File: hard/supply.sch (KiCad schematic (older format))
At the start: 13 parts, among them J2 MicroXNJ

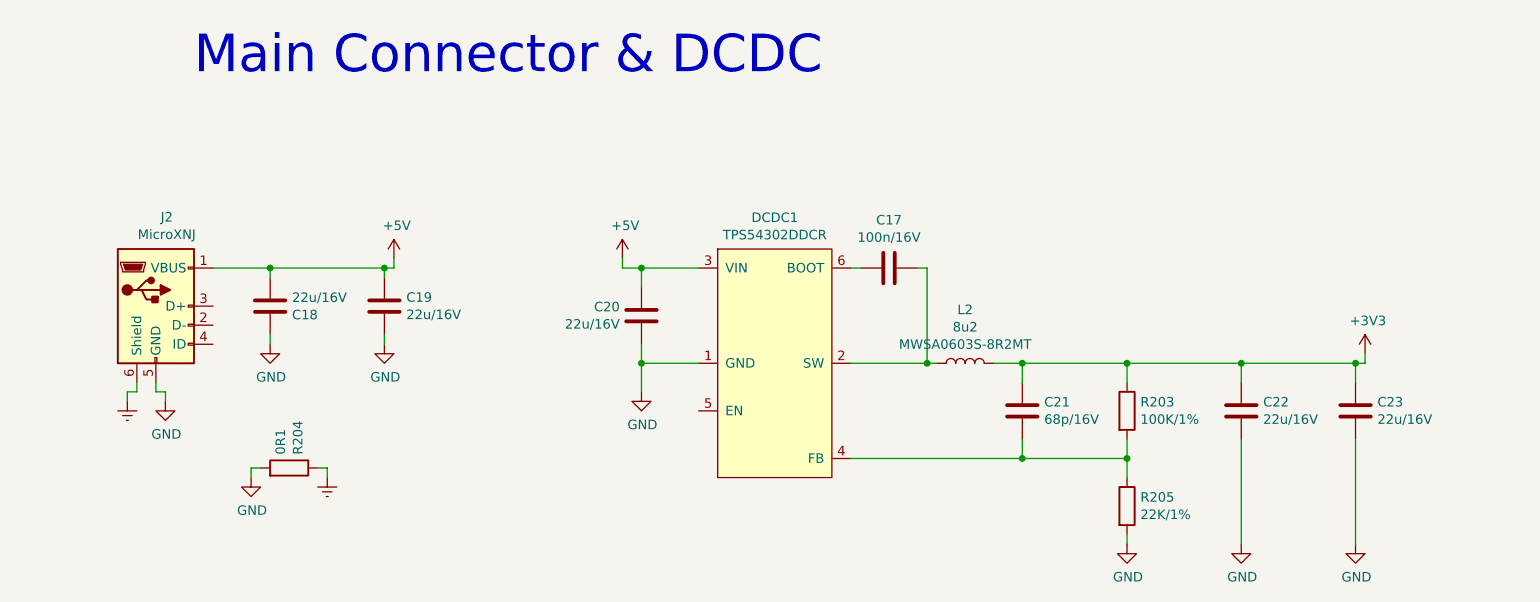
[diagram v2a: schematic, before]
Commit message: general layout update
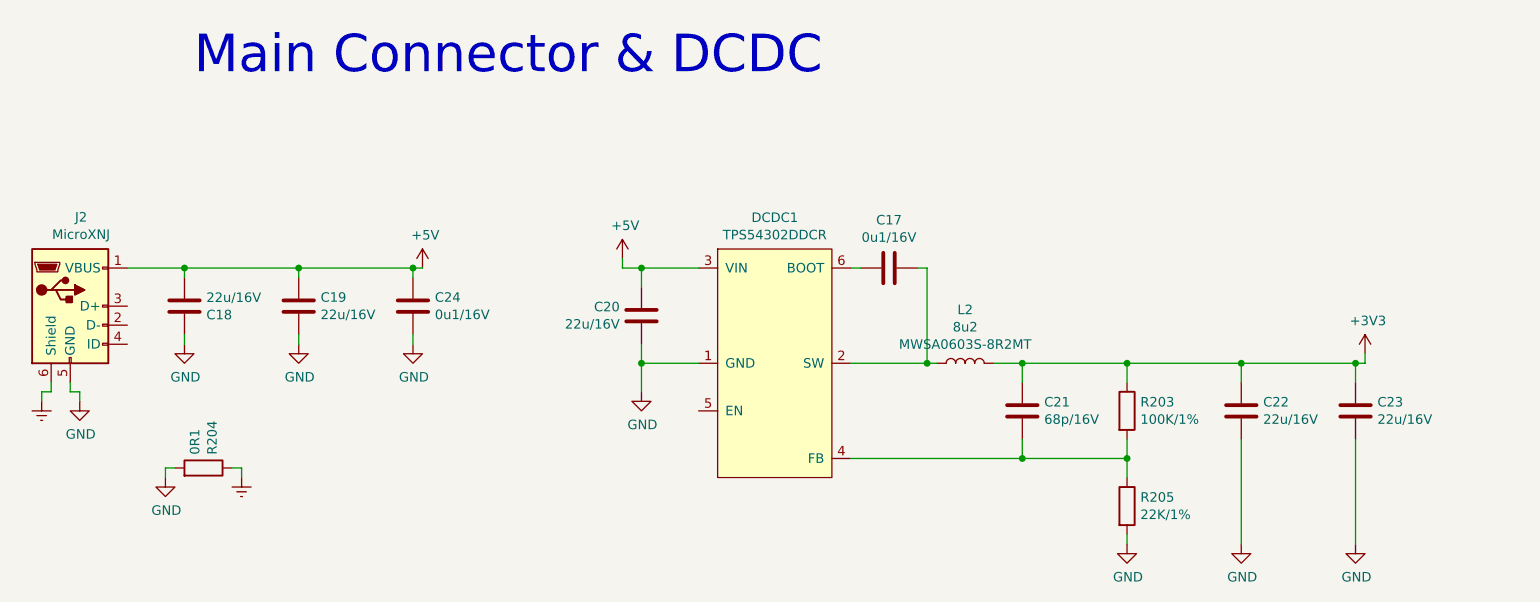
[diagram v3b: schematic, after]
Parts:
- added C24: 0u1/16V, Capacitor_SMD:C_0402_1005Metric, symbol Device:C
- C17: value 100n/16V -> 0u1/16V
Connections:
- net +5V: now also C24.2
- net GND: now also C24.1
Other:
- moved on the sheet: C18, C19, J2, R204
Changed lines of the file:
@@
 P 6750 3400
 F 0 "C17" V 6498 3400 50  0000 C CNN
-F 1 "100n/16V" V 6589 3400 50  0000 C CNN
+F 1 "0u1/16V" V 6589 3400 50  0000 C CNN
 F 2 "Capacitor_SMD:C_0402_1005Metric" H 6788 3250 50  0001 C CNN
 F 3 "~" H 6750 3400 50  0001 C CNN
@@
 L Connector:USB_B_Micro J2
 U 1 1 60567F22
-P 2900 3600
-F 0 "J2" H 2957 4067 50  0000 C CNN
-F 1 "MicroXNJ" H 2957 3976 50  0000 C CNN
-F 2 "led_matrix:Connectors_SHOU HAN_MICRO 4P DIP" H 3050 3550 50  0001 C CNN
-F 3 "1912111437_SHOU-HAN-MICRO-4P-DIP_C456008.pdf" H 3050 3550 50  0001 C CNN
-F 4 "" H 2900 3600 50  0001 C CNN "DigiKey_Part_Number"
-F 5 "" H 2900 3600 50  0001 C CNN "Mouser_Part_Number"
-F 6 "C456008" H 2900 3600 50  0001 C CNN "JLCPCB_Part_Number"
-F 7 "SHOU HAN" H 2900 3600 50  0001 C CNN "MF"
-F 8 "MICRO 4P DIP" H 2900 3600 50  0001 C CNN "MPN"
-F 9 "USB CONNECTORS ROHS" H 2900 3600 50  0001 C CNN "Description"
-	1    2900 3600
+P 2450 3600
+F 0 "J2" H 2507 4067 50  0000 C CNN
+F 1 "MicroXNJ" H 2507 3976 50  0000 C CNN
+F 2 "led_matrix:Connectors_SHOU HAN_MICRO 4P DIP" H 2600 3550 50  0001 C CNN
+F 3 "1912111437_SHOU-HAN-MICRO-4P-DIP_C456008.pdf" H 2600 3550 50  0001 C CNN
+F 4 "" H 2450 3600 50  0001 C CNN "DigiKey_Part_Number"
+F 5 "" H 2450 3600 50  0001 C CNN "Mouser_Part_Number"
+F 6 "C456008" H 2450 3600 50  0001 C CNN "JLCPCB_Part_Number"
+F 7 "SHOU HAN" H 2450 3600 50  0001 C CNN "MF"
+F 8 "MICRO 4P DIP" H 2450 3600 50  0001 C CNN "MPN"
+F 9 "USB CONNECTORS ROHS" H 2450 3600 50  0001 C CNN "Description"
+	1    2450 3600
 	1    0    0    -1
 $EndComp
@@
 L power:+5V #PWR0187
 U 1 1 6056C9AF
-P 4150 3350
-F 0 "#PWR0187" H 4150 3200 50  0001 C CNN
-F 1 "+5V" H 4165 3523 50  0000 C CNN
-F 2 "" H 4150 3350 50  0001 C CNN
-F 3 "" H 4150 3350 50  0001 C CNN
-	1    4150 3350
+P 4300 3400
+F 0 "#PWR0187" H 4300 3250 50  0001 C CNN
+F 1 "+5V" H 4315 3573 50  0000 C CNN
+F 2 "" H 4300 3400 50  0001 C CNN
+F 3 "" H 4300 3400 50  0001 C CNN
+	1    4300 3400
 	1    0    0    -1
 $EndComp
@@
 L power:GND #PWR0194
 U 1 1 6056D447
-P 2950 4100
-F 0 "#PWR0194" H 2950 3850 50  0001 C CNN
-F 1 "GND" H 2955 3927 50  0000 C CNN
-F 2 "" H 2950 4100 50  0001 C CNN
-F 3 "" H 2950 4100 50  0001 C CNN
-	1    2950 4100
+P 2500 4100
+F 0 "#PWR0194" H 2500 3850 50  0001 C CNN
+F 1 "GND" H 2505 3927 50  0000 C CNN
+F 2 "" H 2500 4100 50  0001 C CNN
+F 3 "" H 2500 4100 50  0001 C CNN
+	1    2500 4100
 	1    0    0    -1
 $EndComp
@@
 L Device:R R204
 U 1 1 6056E34B
-P 3600 4450
-F 0 "R204" H 3670 4496 50  0000 L CNN
-F 1 "0R1" H 3670 4405 50  0000 L CNN
-F 2 "Resistor_SMD:R_0805_2012Metric" V 3530 4450 50  0001 C CNN
-F 3 "~" H 3600 4450 50  0001 C CNN
-	1    3600 4450
+P 3150 4450
+F 0 "R204" H 3220 4496 50  0000 L CNN
+F 1 "0R1" H 3220 4405 50  0000 L CNN
+F 2 "Resistor_SMD:R_0805_2012Metric" V 3080 4450 50  0001 C CNN
+F 3 "~" H 3150 4450 50  0001 C CNN
+	1    3150 4450
 	0    1    -1   0
 $EndComp
@@
 L Device:C C18
 U 1 1 60578754
-P 3500 3600
-F 0 "C18" H 3385 3554 50  0000 R CNN
-F 1 "22u/16V" H 3385 3645 50  0000 R CNN
-F 2 "Capacitor_SMD:C_0805_2012Metric" H 3538 3450 50  0001 C CNN
-F 3 "~" H 3500 3600 50  0001 C CNN
-	1    3500 3600
+P 3050 3600
+F 0 "C18" H 2935 3554 50  0000 R CNN
+F 1 "22u/16V" H 2935 3645 50  0000 R CNN
+F 2 "Capacitor_SMD:C_0805_2012Metric" H 3088 3450 50  0001 C CNN
+F 3 "~" H 3050 3600 50  0001 C CNN
+	1    3050 3600
 	-1   0    0    -1
 $EndComp
@@
 L Device:C C19
 U 1 1 6057A690
-P 4100 3600
-F 0 "C19" H 3985 3554 50  0000 R CNN
-F 1 "22u/16V" H 3985 3645 50  0000 R CNN
-F 2 "Capacitor_SMD:C_0805_2012Metric" H 4138 3450 50  0001 C CNN
-F 3 "~" H 4100 3600 50  0001 C CNN
-	1    4100 3600
+P 3650 3600
+F 0 "C19" H 3535 3554 50  0000 R CNN
+F 1 "22u/16V" H 3535 3645 50  0000 R CNN
+F 2 "Capacitor_SMD:C_0805_2012Metric" H 3688 3450 50  0001 C CNN
+F 3 "~" H 3650 3600 50  0001 C CNN
+	1    3650 3600
 	-1   0    0    1
 $EndComp
 Wire Wire Line
-	4150 3400 4150 3350
-Wire Wire Line
-	3200 3400 3500 3400
-Wire Wire Line
-	4100 3450 4100 3400
-Connection ~ 4100 3400
-Wire Wire Line
-	4100 3400 4150 3400
-Wire Wire Line
-	3500 3450 3500 3400
-Connection ~ 3500 3400
-Wire Wire Line
-	3500 3400 4100 3400
+	2750 3400 3050 3400
+Wire Wire Line
+	3650 3450 3650 3400
+Connection ~ 3650 3400
+Wire Wire Line
+	3050 3450 3050 3400
+Connection ~ 3050 3400
+Wire Wire Line
+	3050 3400 3650 3400
 $Comp
 L power:GND #PWR0189
 U 1 1 6057E614
-P 3500 3800
-F 0 "#PWR0189" H 3500 3550 50  0001 C CNN
-F 1 "GND" H 3505 3627 50  0000 C CNN
-F 2 "" H 3500 3800 50  0001 C CNN
-F 3 "" H 3500 3800 50  0001 C CNN
-	1    3500 3800
+P 3050 3800
+F 0 "#PWR0189" H 3050 3550 50  0001 C CNN
+F 1 "GND" H 3055 3627 50  0000 C CNN
+F 2 "" H 3050 3800 50  0001 C CNN
+F 3 "" H 3050 3800 50  0001 C CNN
+	1    3050 3800
 	1    0    0    -1
 $EndComp
@@
 L power:GND #PWR0190
 U 1 1 6057ED88
-P 4100 3800
-F 0 "#PWR0190" H 4100 3550 50  0001 C CNN
-F 1 "GND" H 4105 3627 50  0000 C CNN
-F 2 "" H 4100 3800 50  0001 C CNN
-F 3 "" H 4100 3800 50  0001 C CNN
-	1    4100 3800
-	1    0    0    -1
-$EndComp
-Wire Wire Line
-	3500 3800 3500 3750
-Wire Wire Line
-	4100 3800 4100 3750
+P 3650 3800
+F 0 "#PWR0190" H 3650 3550 50  0001 C CNN
+F 1 "GND" H 3655 3627 50  0000 C CNN
+F 2 "" H 3650 3800 50  0001 C CNN
+F 3 "" H 3650 3800 50  0001 C CNN
+	1    3650 3800
+	1    0    0    -1
+$EndComp
+Wire Wire Line
+	3050 3800 3050 3750
+Wire Wire Line
+	3650 3800 3650 3750
 $Comp
 L power:Earth #PWR0196
 U 1 1 614EE00A
-P 3800 4500
-F 0 "#PWR0196" H 3800 4250 50  0001 C CNN
-F 1 "Earth" H 3800 4350 50  0001 C CNN
-F 2 "" H 3800 4500 50  0001 C CNN
-F 3 "~" H 3800 4500 50  0001 C CNN
-	1    3800 4500
-	1    0    0    -1
-$EndComp
-Wire Wire Line
-	2900 4000 2900 4050
+P 3350 4500
+F 0 "#PWR0196" H 3350 4250 50  0001 C CNN
+F 1 "Earth" H 3350 4350 50  0001 C CNN
+F 2 "" H 3350 4500 50  0001 C CNN
+F 3 "~" H 3350 4500 50  0001 C CNN
+	1    3350 4500
+	1    0    0    -1
+$EndComp
+Wire Wire Line
+	2450 4000 2450 4050
 $Comp
 L power:GND #PWR0195
 U 1 1 614F0A85
-P 3400 4500
-F 0 "#PWR0195" H 3400 4250 50  0001 C CNN
-F 1 "GND" H 3405 4327 50  0000 C CNN
-F 2 "" H 3400 4500 50  0001 C CNN
-F 3 "" H 3400 4500 50  0001 C CNN
-	1    3400 4500
+P 2950 4500
+F 0 "#PWR0195" H 2950 4250 50  0001 C CNN
+F 1 "GND" H 2955 4327 50  0000 C CNN
+F 2 "" H 2950 4500 50  0001 C CNN
+F 3 "" H 2950 4500 50  0001 C CNN
+	1    2950 4500
 	1    0    0    -1
 $EndComp
@@
 L power:Earth #PWR0193
 U 1 1 614F2C5D
-P 2750 4100
-F 0 "#PWR0193" H 2750 3850 50  0001 C CNN
-F 1 "Earth" H 2750 3950 50  0001 C CNN
-F 2 "" H 2750 4100 50  0001 C CNN
-F 3 "~" H 2750 4100 50  0001 C CNN
-	1    2750 4100
-	1    0    0    -1
-$EndComp
-Wire Wire Line
-	2800 4000 2800 4050
-Wire Wire Line
-	2800 4050 2750 4050
-Wire Wire Line
-	2750 4050 2750 4100
-Wire Wire Line
-	2900 4050 2950 4050
-Wire Wire Line
-	2950 4050 2950 4100
-Wire Wire Line
-	3400 4500 3400 4450
-Wire Wire Line
-	3400 4450 3450 4450
-Wire Wire Line
-	3750 4450 3800 4450
-Wire Wire Line
-	3800 4450 3800 4500
+P 2300 4100
+F 0 "#PWR0193" H 2300 3850 50  0001 C CNN
+F 1 "Earth" H 2300 3950 50  0001 C CNN
+F 2 "" H 2300 4100 50  0001 C CNN
+F 3 "~" H 2300 4100 50  0001 C CNN
+	1    2300 4100
+	1    0    0    -1
+$EndComp
+Wire Wire Line
+	2350 4000 2350 4050
+Wire Wire Line
+	2350 4050 2300 4050
+Wire Wire Line
+	2300 4050 2300 4100
+Wire Wire Line
+	2450 4050 2500 4050
+Wire Wire Line
+	2500 4050 2500 4100
+Wire Wire Line
+	2950 4500 2950 4450
+Wire Wire Line
+	2950 4450 3000 4450
+Wire Wire Line
+	3300 4450 3350 4450
+Wire Wire Line
+	3350 4450 3350 4500
 Wire Wire Line
 	8600 3900 9200 3900
@@
 Text Notes 3100 2400 0    197  ~ 0
 Main Connector & DCDC
+Wire Wire Line
+	3650 3400 4250 3400
+Wire Wire Line
+	4250 3450 4250 3400
+Connection ~ 4250 3400
+Wire Wire Line
+	4250 3400 4300 3400
+$Comp
+L power:GND #PWR0200
+U 1 1 613BB852
+P 4250 3800
+F 0 "#PWR0200" H 4250 3550 50  0001 C CNN
+F 1 "GND" H 4255 3627 50  0000 C CNN
+F 2 "" H 4250 3800 50  0001 C CNN
+F 3 "" H 4250 3800 50  0001 C CNN
+	1    4250 3800
+	1    0    0    -1
+$EndComp
+Wire Wire Line
+	4250 3750 4250 3800
+$Comp
+L Device:C C24
+U 1 1 613D470A
+P 4250 3600
+F 0 "C24" H 4135 3554 50  0000 R CNN
+F 1 "0u1/16V" H 4135 3645 50  0000 R CNN
+F 2 "Capacitor_SMD:C_0402_1005Metric" H 4288 3450 50  0001 C CNN
+F 3 "~" H 4250 3600 50  0001 C CNN
+	1    4250 3600
+	-1   0    0    1
+$EndComp
 $EndSCHEMATC

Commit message: release candidate. ready for review by @lukekaese
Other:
- moved on the sheet: C17, C20, C21, C22, C23, DCDC1, L2, R203, R204, R205

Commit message: attribute naming update
JLCPCB_Part_Number -> LCSC
DigiKey_Part_Number -> DigiKey
Mouser_Part_Number -> Mouser
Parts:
- DCDC1: DigiKey (none) -> 296-46237-1-ND; DigiKey_Part_Number 296-46237-1-ND -> (none); JLCPCB_Part_Number C311983 -> (none); LCSC (none) -> C311983
- J2: JLCPCB_Part_Number C456008 -> (none); LCSC (none) -> C456008
- L2: JLCPCB_Part_Number C408450 -> (none); LCSC (none) -> C408450
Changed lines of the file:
@@
 F 2 "Package_TO_SOT_SMD:SOT-23-6_Handsoldering" H 6550 3300 50  0001 C CNN
 F 3 "https://www.ti.com/lit/gpn/TPS54302" H 6550 3300 50  0001 C CNN
-F 4 "296-46237-1-ND" H 6550 3300 50  0001 C CNN "DigiKey_Part_Number"
-F 5 "C311983" H 6550 3300 50  0001 C CNN "JLCPCB_Part_Number"
+F 4 "296-46237-1-ND" H 6550 3300 50  0001 C CNN "DigiKey"
+F 5 "C311983" H 6550 3300 50  0001 C CNN "LCSC"
 F 6 "Texas Instruments" H 6550 3300 50  0001 C CNN "MF"
 F 7 "TPS54302DDCR" H 6550 3300 50  0001 C CNN "MPN"
@@
 F 2 "led_matrix:L_Sunking_MWSA0603S" H 7550 3900 50  0001 C CNN
 F 3 "https://datasheet.lcsc.com/szlcsc/1912111437_Sunlord-MWSA0603S-8R2MT_C408450.pdf" H 7550 3900 50  0001 C CNN
-F 4 "C408450" H 7550 3900 50  0001 C CNN "JLCPCB_Part_Number"
+F 4 "C408450" H 7550 3900 50  0001 C CNN "LCSC"
 F 5 "Sunlord" H 7550 3900 50  0001 C CNN "MF"
 F 6 "MWSA0603S-8R2MT" V 7649 3900 50  0000 C CNN "MPN"
@@
 F 2 "led_matrix:Connectors_SHOU HAN_MICRO 4P DIP" H 2600 3550 50  0001 C CNN
 F 3 "https://datasheet.lcsc.com/szlcsc/1912111437_SHOU-HAN-MICRO-4P-DIP_C456008.pdf" H 2600 3550 50  0001 C CNN
-F 4 "" H 2450 3600 50  0001 C CNN "DigiKey_Part_Number"
-F 5 "" H 2450 3600 50  0001 C CNN "Mouser_Part_Number"
-F 6 "C456008" H 2450 3600 50  0001 C CNN "JLCPCB_Part_Number"
+F 4 "" H 2450 3600 50  0001 C CNN "DigiKey"
+F 5 "" H 2450 3600 50  0001 C CNN "Mouser"
+F 6 "C456008" H 2450 3600 50  0001 C CNN "LCSC"
 F 7 "SHOU HAN" H 2450 3600 50  0001 C CNN "MF"
 F 8 "MICRO 4P DIP" H 2450 3600 50  0001 C CNN "MPN"
